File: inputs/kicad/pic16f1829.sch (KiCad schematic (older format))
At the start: 3 parts, among them P7 CONN_01X05, U1 PIC16F1829LIN

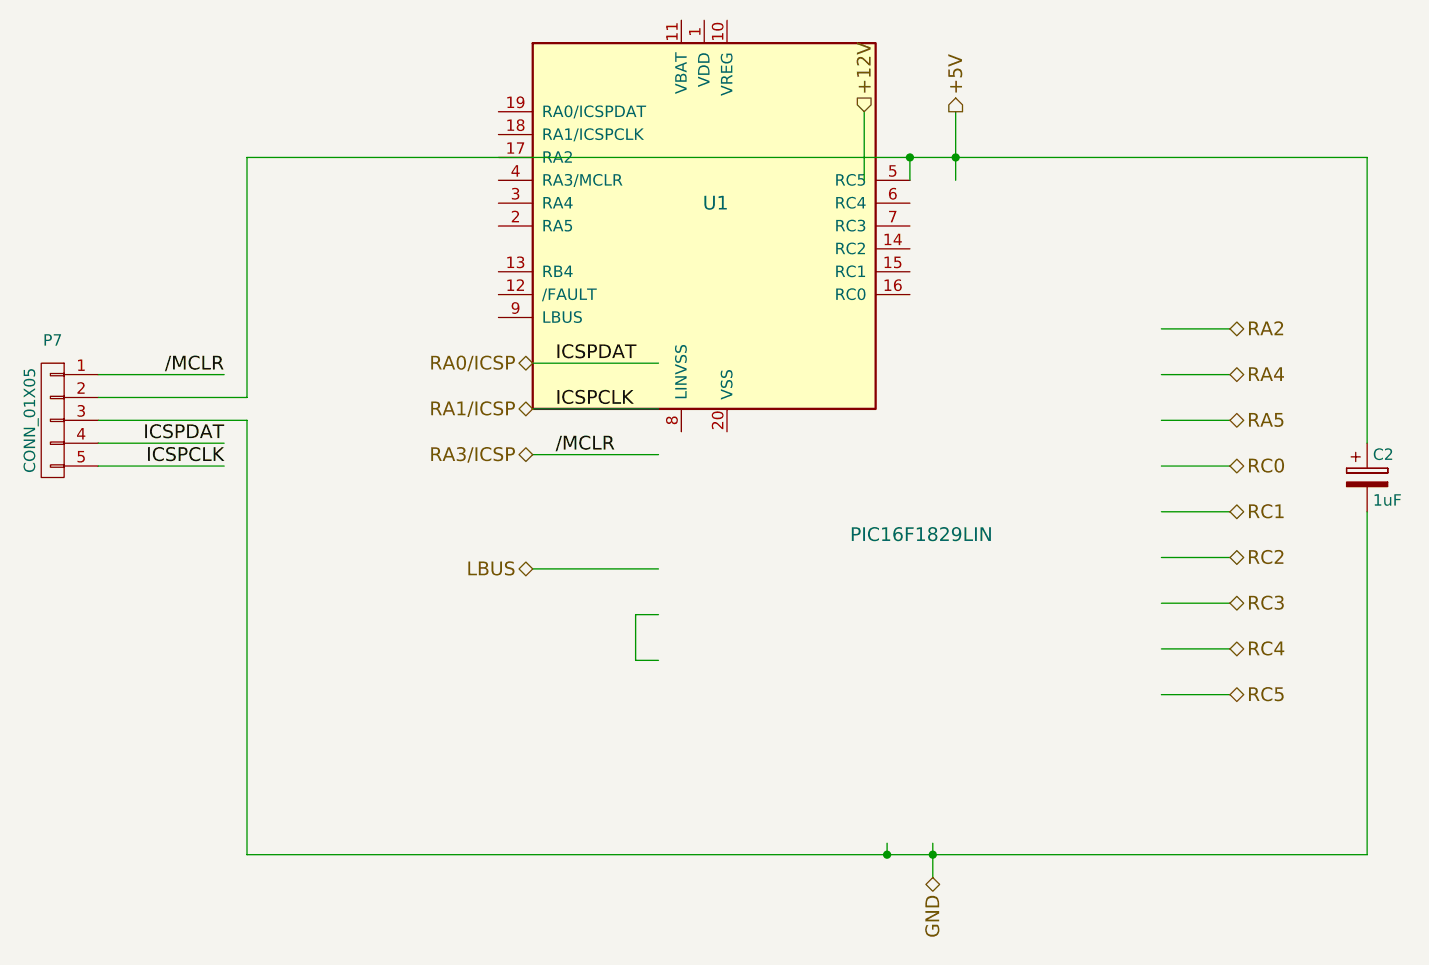
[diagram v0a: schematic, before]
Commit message: [inputs] Updating to use standard libraries
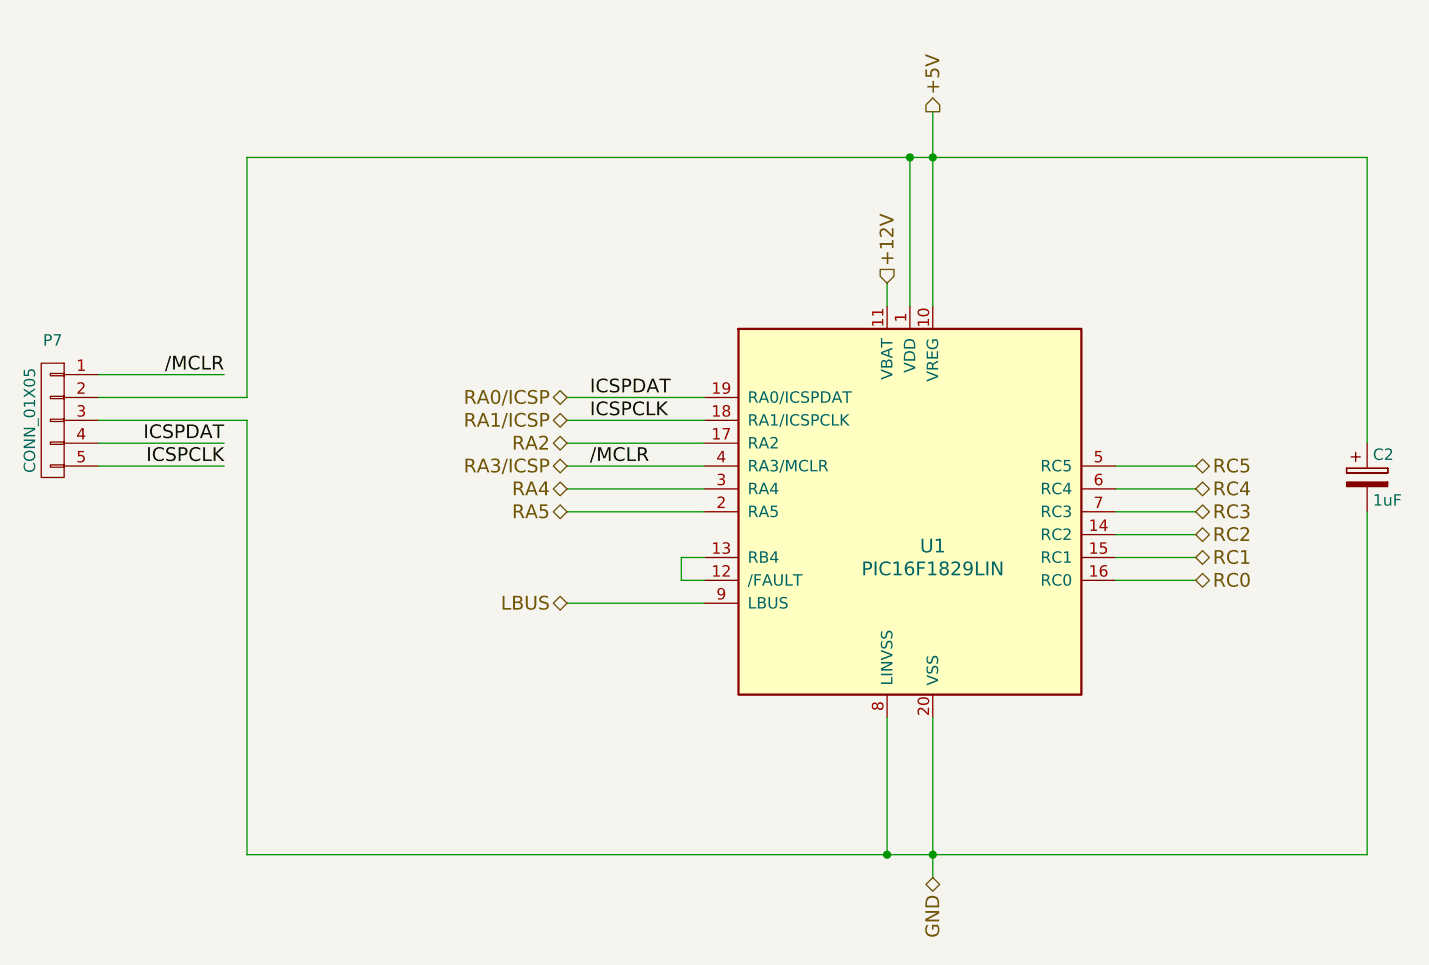
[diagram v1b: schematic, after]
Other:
- moved on the sheet: U1
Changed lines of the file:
@@
 EESchema Schematic File Version 2
+LIBS:microchip_pic16mcu
 LIBS:power
 LIBS:device
@@
 LIBS:valves
 LIBS:inputs
-LIBS:fluffy-potato
+LIBS:switches
+LIBS:rfcom
 LIBS:inputs-cache
 EELAYER 25 0
@@
 L PIC16F1829LIN U1
 U 1 1 584DAA7D
-P 5400 2550
-F 0 "U1" H 5450 2650 60  0000 C CNN
-F 1 "PIC16F1829LIN" H 6350 1200 60  0000 C CNN
-F 2 "Housings_SSOP:SSOP-20_5.3x7.2mm_Pitch0.65mm" H 5400 2550 60  0001 C CNN
-F 3 "http://ww1.microchip.com/downloads/en/DeviceDoc/41673A.pdf" H 5400 2550 60  0001 C CNN
-F 4 "PIC16F1829LIN-I/SS-ND" H 5400 2550 60  0001 C CNN "DIGIKEY"
-	1    5400 2550
+P 6300 3800
+AR Path="/584DAA7D" Ref="U1"  Part="1"
+AR Path="/584DA63A/584DAA7D" Ref="U1"  Part="1"
+F 0 "U1" H 6400 3650 60  0000 C CNN
+F 1 "PIC16F1829LIN" H 6400 3550 60  0000 C CNN
+F 2 "Housings_SSOP:SSOP-20_5.3x7.2mm_Pitch0.65mm" H 6300 3800 60  0001 C CNN
+F 3 "http://ww1.microchip.com/downloads/en/DeviceDoc/41673A.pdf" H 6300 3800 60  0001 C CNN
+F 4 "PIC16F1829LIN-I/SS-ND" H 6300 3800 60  0001 C CNN "DIGIKEY"
+	1    6300 3800
 	1    0    0    -1
 $EndComp
@@
 	1    0    0    -1
 $EndComp
-Text Label 4750 3550 0    60   ~ 0
+Text Label 4900 3600 0    60   ~ 0
 /MCLR
-Text Label 4750 3150 0    60   ~ 0
+Text Label 4900 3300 0    60   ~ 0
 ICSPDAT
-Text Label 4750 3350 0    60   ~ 0
+Text Label 4900 3400 0    60   ~ 0
 ICSPCLK
 $Comp
@@
 ICSPCLK
 Wire Wire Line
-	4650 3550 5200 3550
+	4800 3600 5400 3600
 Wire Wire Line
-	4650 3150 5200 3150
+	4800 3300 5400 3300
 Wire Wire Line
-	4650 3350 5200 3350
+	4800 3400 5400 3400
 Wire Wire Line
-	5200 4250 5100 4250
+	6200 4700 6200 5300
 Wire Wire Line
-	5100 4250 5100 4450
+	6400 4700 6400 5400
 Wire Wire Line
-	5100 4450 5200 4450
+	6200 2800 6200 2900
 Wire Wire Line
-	6200 5250 6200 5300
-Wire Wire Line
-	6400 5250 6400 5400
-Wire Wire Line
-	6100 2050 6100 2350
-Wire Wire Line
-	6300 2350 6300 2250
+	6300 2250 6300 2900
 Wire Wire Line
 	3400 2250 8300 2250
 Wire Wire Line
-	6500 2050 6500 2350
+	6400 2050 6400 2900
 Wire Wire Line
 	2750 3200 3300 3200
@@
 	3400 5300 8300 5300
 Connection ~ 6400 5300
-Text HLabel 7700 3000 2    60   BiDi ~ 0
+Text HLabel 4800 3500 0    60   BiDi ~ 0
 RA2
-Text HLabel 7700 3200 2    60   BiDi ~ 0
+Text HLabel 4800 3700 0    60   BiDi ~ 0
 RA4
-Text HLabel 7700 3400 2    60   BiDi ~ 0
+Text HLabel 4800 3800 0    60   BiDi ~ 0
 RA5
-Text HLabel 7700 3600 2    60   BiDi ~ 0
+Text HLabel 7550 4100 2    60   BiDi ~ 0
 RC0
-Text HLabel 7700 3800 2    60   BiDi ~ 0
+Text HLabel 7550 4000 2    60   BiDi ~ 0
 RC1
-Text HLabel 7700 4000 2    60   BiDi ~ 0
+Text HLabel 7550 3900 2    60   BiDi ~ 0
 RC2
-Text HLabel 7700 4200 2    60   BiDi ~ 0
+Text HLabel 7550 3800 2    60   BiDi ~ 0
 RC3
-Text HLabel 7700 4400 2    60   BiDi ~ 0
+Text HLabel 7550 3700 2    60   BiDi ~ 0
 RC4
-Text HLabel 7700 4600 2    60   BiDi ~ 0
+Text HLabel 7550 3600 2    60   BiDi ~ 0
 RC5
-Text HLabel 4650 3150 0    60   BiDi ~ 0
+Text HLabel 4800 3300 0    60   BiDi ~ 0
 RA0/ICSP
-Text HLabel 4650 3350 0    60   BiDi ~ 0
+Text HLabel 4800 3400 0    60   BiDi ~ 0
 RA1/ICSP
-Text HLabel 4650 3550 0    60   BiDi ~ 0
+Text HLabel 4800 3600 0    60   BiDi ~ 0
 RA3/ICSP
 Wire Wire Line
-	7700 3000 7400 3000
+	4800 3500 5400 3500
 Wire Wire Line
-	7400 3200 7700 3200
+	5400 3700 4800 3700
 Wire Wire Line
-	7700 3400 7400 3400
+	4800 3800 5400 3800
 Wire Wire Line
-	7400 3600 7700 3600
+	7200 4100 7550 4100
 Wire Wire Line
-	7400 3800 7700 3800
+	7200 4000 7550 4000
 Wire Wire Line
-	7400 4000 7700 4000
+	7200 3900 7550 3900
 Wire Wire Line
-	7400 4200 7700 4200
+	7200 3800 7550 3800
 Wire Wire Line
-	7400 4400 7700 4400
+	7200 3700 7550 3700
 Wire Wire Line
-	7400 4600 7700 4600
-Text HLabel 4650 4050 0    60   BiDi ~ 0
+	7200 3600 7550 3600
+Text HLabel 4800 4200 0    60   BiDi ~ 0
 LBUS
 Wire Wire Line
-	4650 4050 5200 4050
-Text HLabel 6500 2050 1    60   Output ~ 0
+	4800 4200 5400 4200
+Text HLabel 6400 2050 1    60   Output ~ 0
 +5V
-Text HLabel 6100 2050 1    60   Input ~ 0
+Text HLabel 6200 2800 1    60   Input ~ 0
 +12V
 Wire Wire Line
@@
 Wire Wire Line
 	8300 2250 8300 3500
-Connection ~ 6500 2250
+Connection ~ 6400 2250
 Connection ~ 6300 2250
 Connection ~ 6200 5300
 Text HLabel 6400 5400 3    60   BiDi ~ 0
 GND
+Wire Wire Line
+	5400 4100 5300 4100
+Wire Wire Line
+	5300 4100 5300 4000
+Wire Wire Line
+	5300 4000 5400 4000
 $EndSCHEMATC
